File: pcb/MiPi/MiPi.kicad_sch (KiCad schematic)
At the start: 29 parts, among them SW1 SW_Push, SW2 SW_Push, U1 RP2350_60QFN, Y1 Crystal_GND24

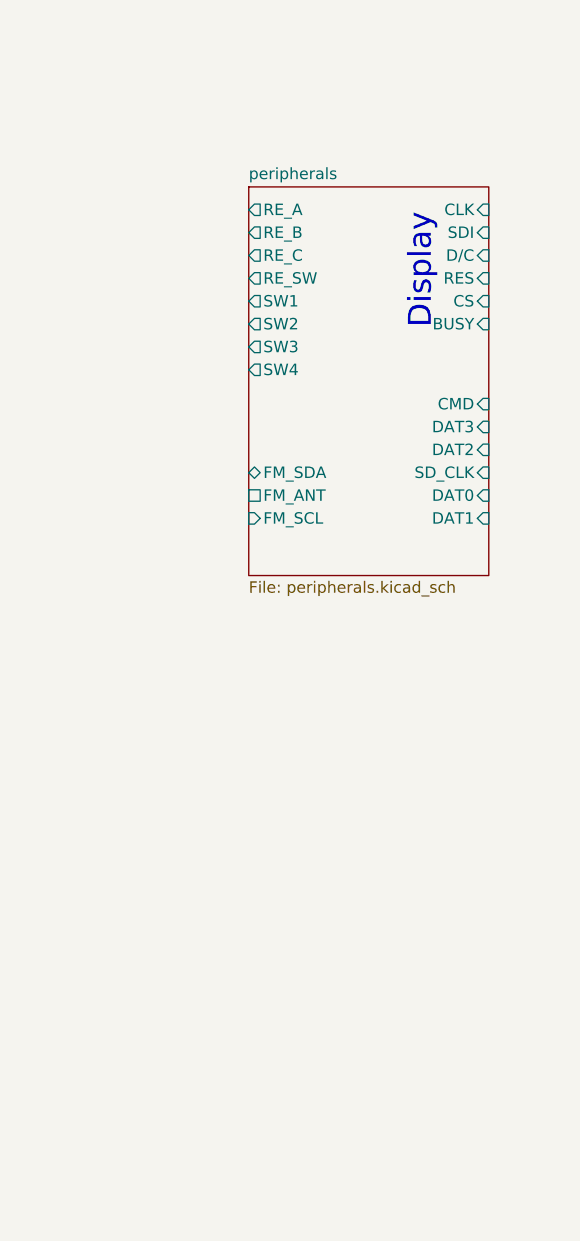
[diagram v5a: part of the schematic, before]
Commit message: Peripherals sheet basically finished; Needs a check.
Added an analog switch for selecting between the radio audio and the RP2350's audio; A headphone audio amp and an audio jack
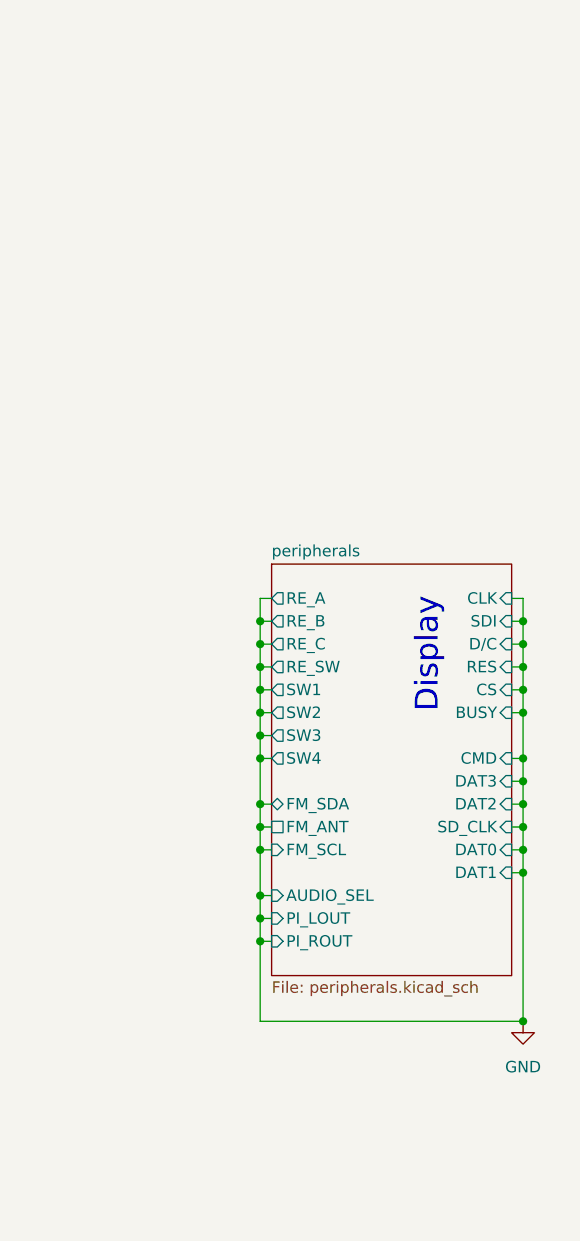
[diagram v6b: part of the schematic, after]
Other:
- sheet peripherals ports: added AUDIO_SEL, PI_LOUT, PI_ROUT; removed none

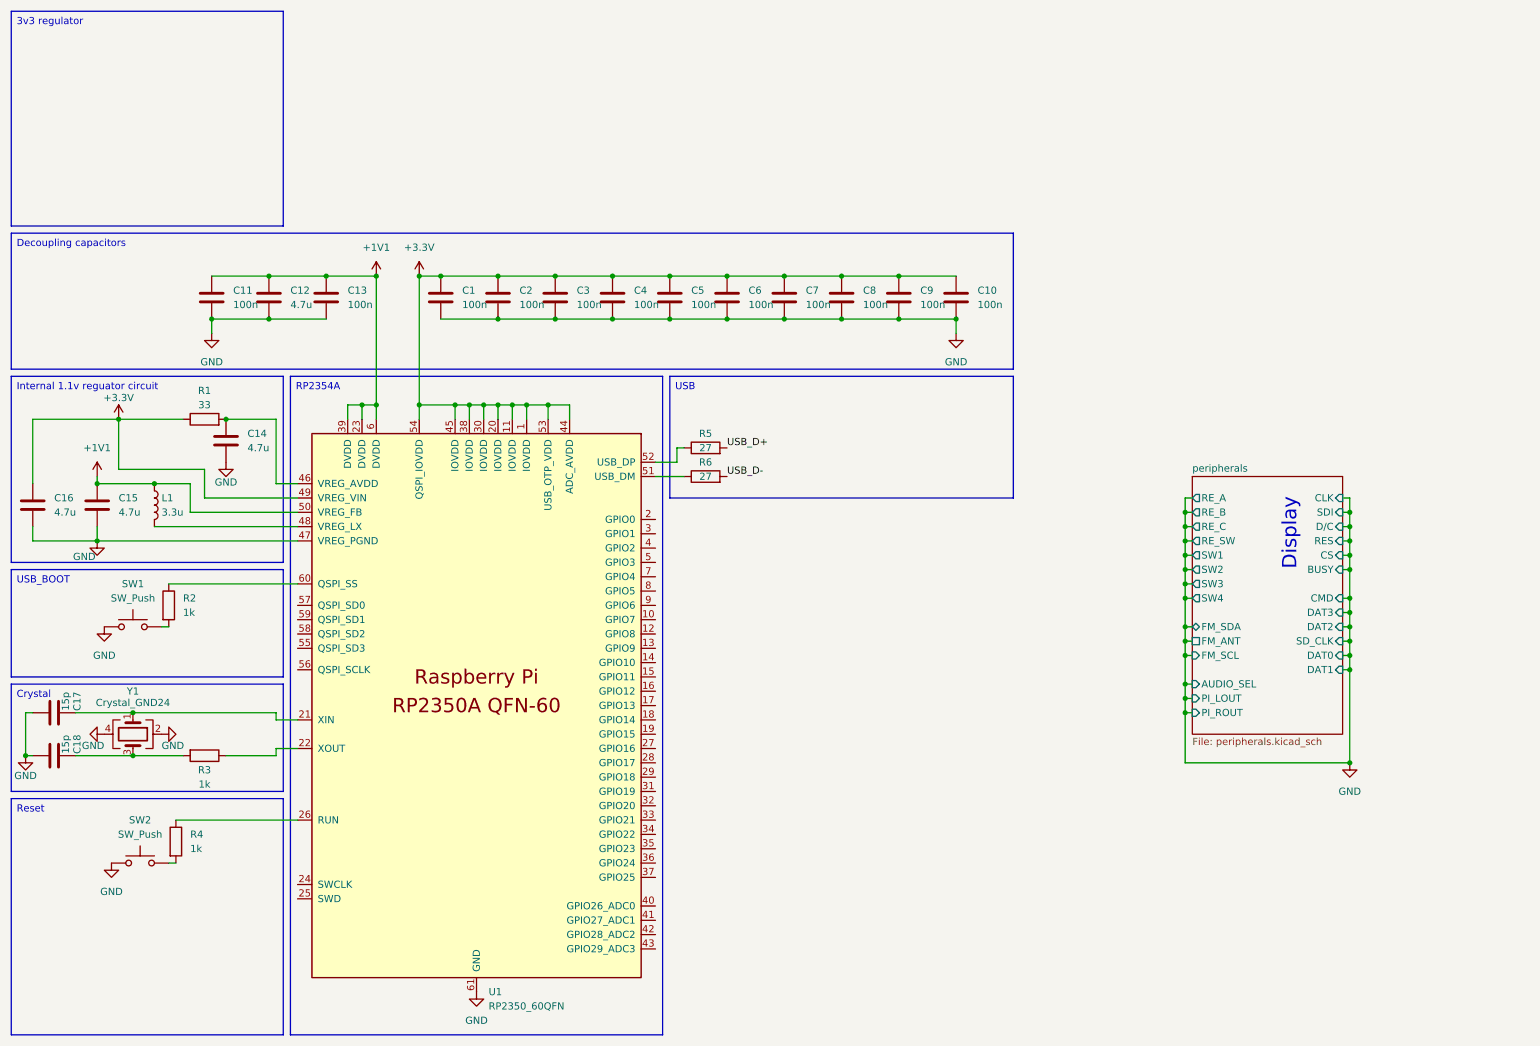
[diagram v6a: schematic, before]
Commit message: Added USB-C connector
Remaining To Do-s: connect the peripherals to GPIO, figure out if and how to implement a rechargeable LiPo battery, 3v3 regulator, and check the all the circuit again!
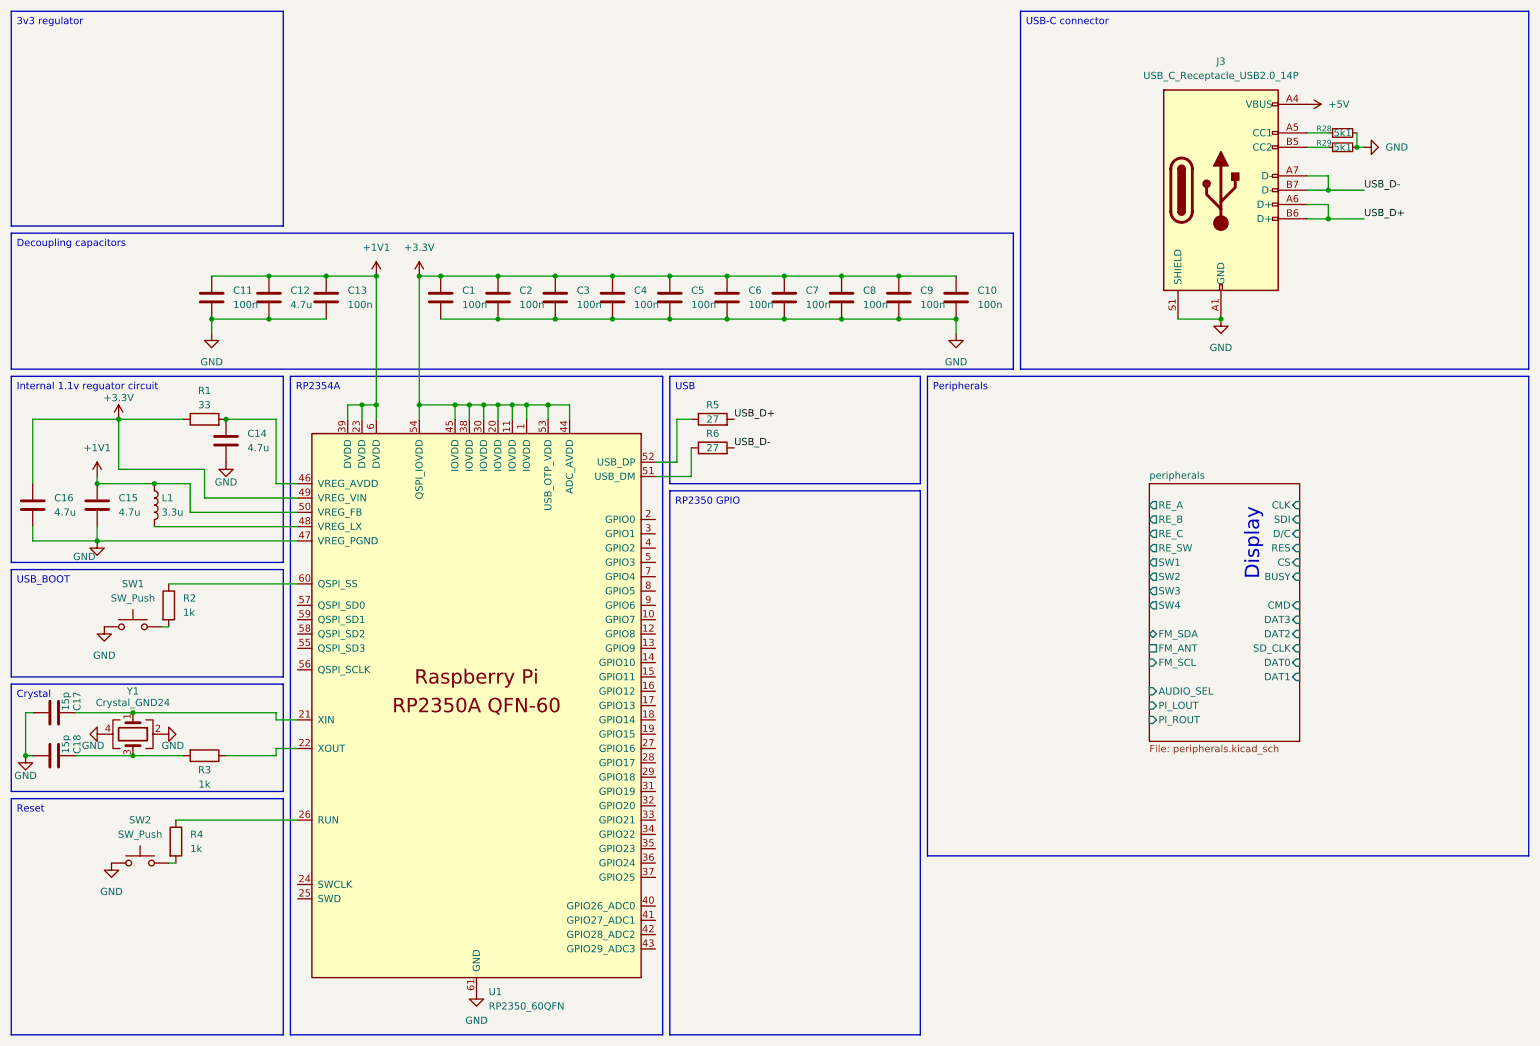
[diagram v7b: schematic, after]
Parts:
- added J3: USB_C_Receptacle_USB2.0_14P, symbol Connector:USB_C_Receptacle_USB2.0_14P
- added R28, R29: 5k1, symbol Device:R_Small
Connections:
- net GND: now also J3.A1 (GND), J3.A12 (GND), J3.B1 (GND), J3.B12 (GND), J3.S1 (SHIELD), R28.2, R29.2
- net USB_D+: now also J3.A6 (D+), J3.B6 (D+)
- net USB_D-: now also J3.A7 (D-), J3.B7 (D-)
- new net: J3.A5 (CC1), R28.1
- new net: J3.B5 (CC2), R29.1
- new net +5V: J3.A4 (VBUS), J3.A9 (VBUS), J3.B4 (VBUS), J3.B9 (VBUS)
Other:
- moved on the sheet: R5, R6

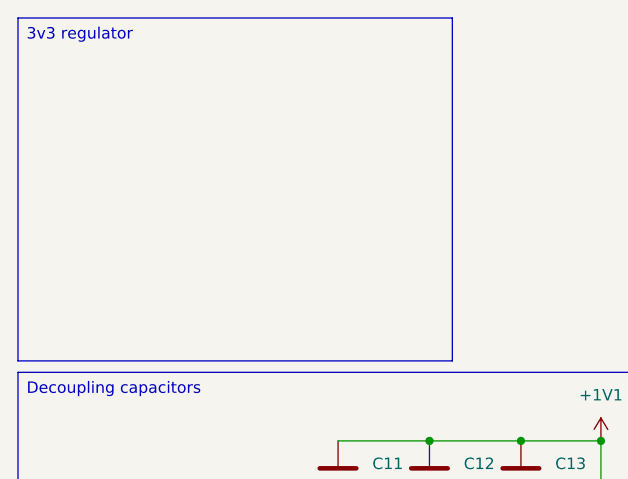
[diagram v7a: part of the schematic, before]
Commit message: Started routing the PCB
Done with the RP2350's decoupling caps, buttons and USB-C connector; Done with the display's driving circuit.
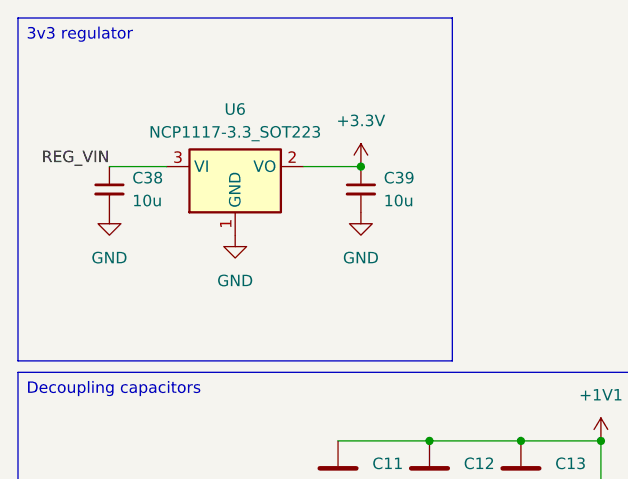
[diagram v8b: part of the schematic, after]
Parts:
- added C38, C39: 10u, Capacitor_SMD:C_0402_1005Metric, symbol Device:C_Small
- added U6: NCP1117-3.3_SOT223, Package_TO_SOT_SMD:SOT-223-3_TabPin2, symbol Regulator_Linear:NCP1117-3.3_SOT223
- C1, C10, C11, C12, C13, C14, C15, C16, C17, C18, C2, C3, C4, C5, C6, C7, C8, C9: footprint (none) -> Capacitor_SMD:C_0402_1005Metric
- J3: footprint (none) -> Connector_USB:USB_C_Receptacle_Amphenol_124019772112A
- L1: footprint (none) -> RP2350_60QFN_minimal:L_pol_2016
- R1, R2, R28, R29, R3, R4, R5, R6: footprint (none) -> Resistor_SMD:R_0402_1005Metric
- SW1, SW2: footprint (none) -> Button_Switch_SMD:SW_Push_1P1T_NO_CK_KMR2
- Y1: footprint (none) -> Crystal:Crystal_SMD_Abracon_ABM8G-4Pin_3.2x2.5mm
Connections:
- net +3.3V: now also C39.1, U6.2 (VO)
- net GND: now also C38.2, C39.2, U6.1 (GND)
- new net REG_VIN: C38.1, U6.3 (VI)
